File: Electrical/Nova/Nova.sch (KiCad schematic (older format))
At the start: 4 parts

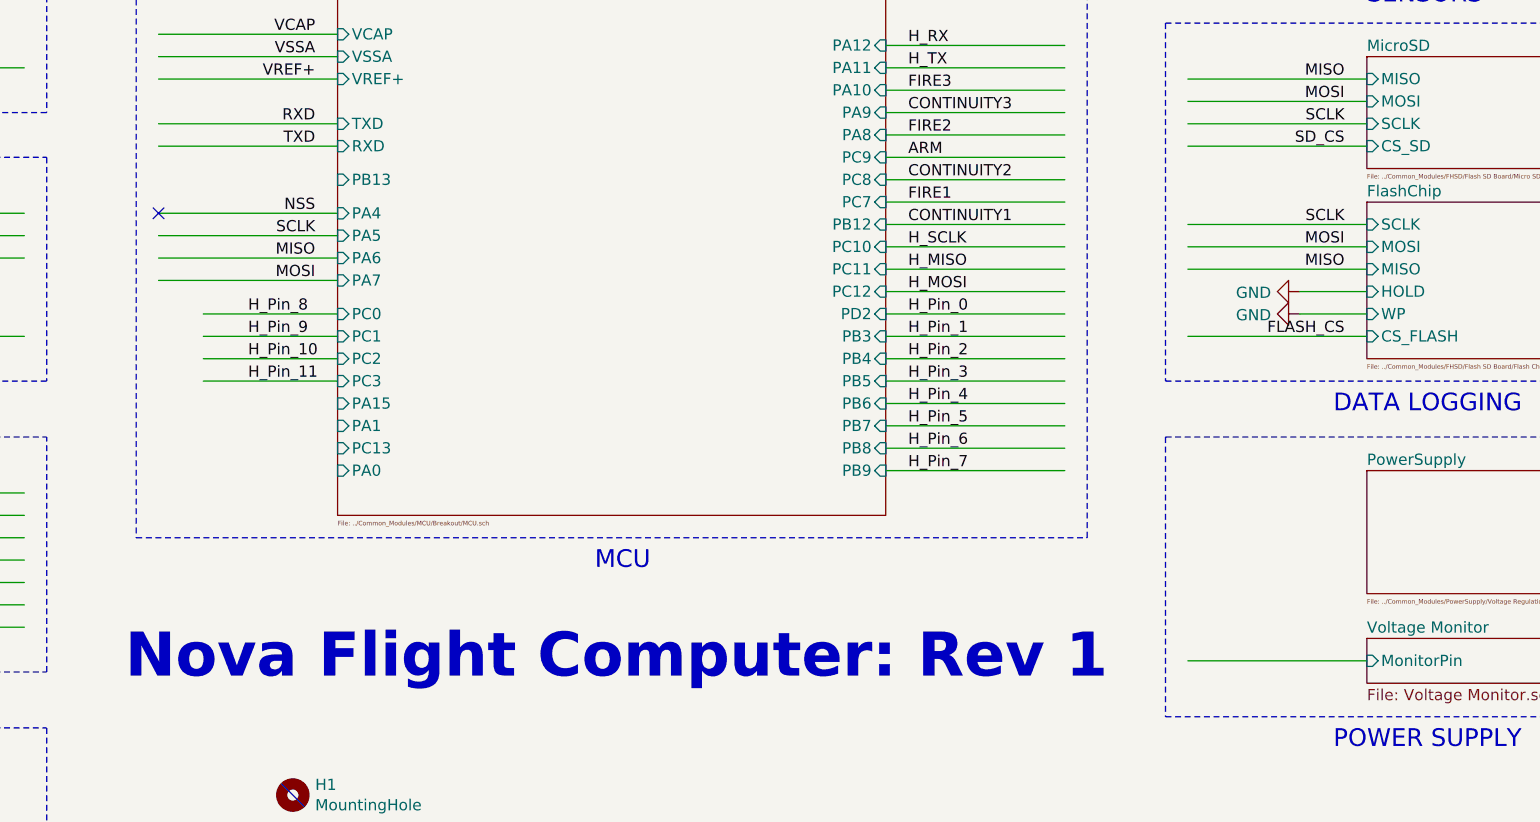
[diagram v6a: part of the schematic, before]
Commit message: Minor Bug Fixes for PCB
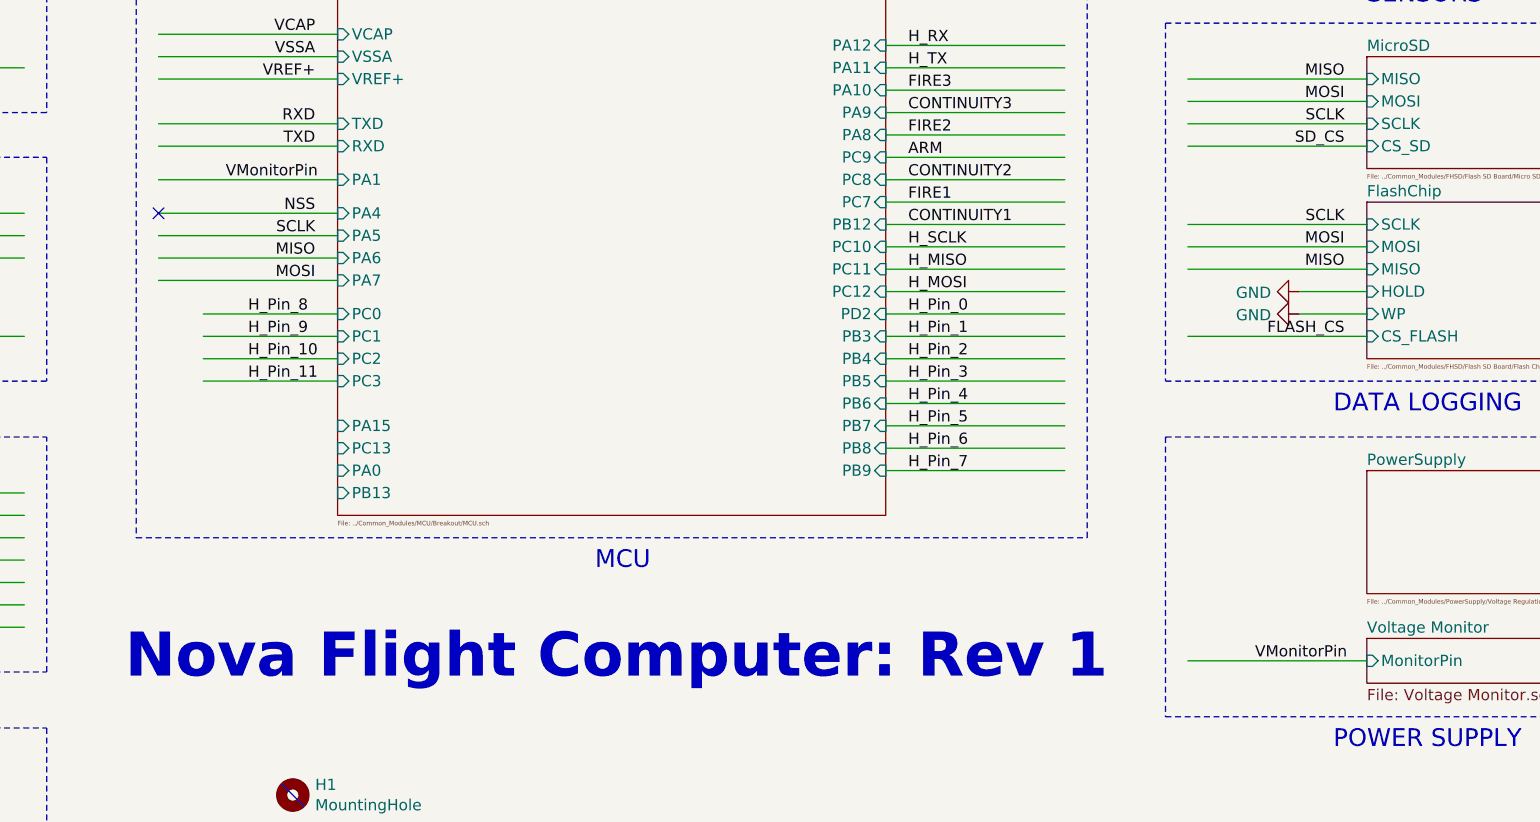
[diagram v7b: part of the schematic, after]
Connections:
- net labels added: VMonitorPin
- wire segments 120 -> 121
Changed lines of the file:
@@
 F25 "PA10" I R 6750 3350 50
 F26 "PB10" I R 6750 2250 50
-F27 "PB13" I L 4300 3750 50
+F27 "PB13" I L 4300 5150 50
 F28 "PB14" I R 6750 2700 50
 F29 "PB15" I R 6750 2800 50
@@
 F43 "PD2" I R 6750 4350 50
 F44 "PA0" I L 4300 5050 50
-F45 "PA1" I L 4300 4850 50
+F45 "PA1" I L 4300 3750 50
 F46 "PA11" I R 6750 3250 50
-F47 "PA15" I L 4300 4750 50
+F47 "PA15" I L 4300 4850 50
 F48 "PB3" I R 6750 4450 50
 F49 "PB4" I R 6750 4550 50
@@
 MOSI
 $Comp
-L power:GND #PWR?
+L power:GND #PWR0122
 U 1 1 5FA3956D
 P 8600 4250
-F 0 "#PWR?" H 8600 4000 50  0001 C CNN
+F 0 "#PWR0122" H 8600 4000 50  0001 C CNN
 F 1 "GND" V 8605 4122 50  0000 R CNN
 F 2 "" H 8600 4250 50  0001 C CNN
@@
 $EndComp
 $Comp
-L power:GND #PWR?
+L power:GND #PWR0123
 U 1 1 5FA39A9B
 P 8600 4350
-F 0 "#PWR?" H 8600 4100 50  0001 C CNN
+F 0 "#PWR0123" H 8600 4100 50  0001 C CNN
 F 1 "GND" V 8605 4222 50  0000 R CNN
 F 2 "" H 8600 4350 50  0001 C CNN
@@
 Wire Wire Line
 	8600 4350 8900 4350
+Text Label 8400 5900 0    50   ~ 0
+VMonitorPin
+Wire Wire Line
+	4300 3750 3500 3750
+Text Label 3800 3750 0    50   ~ 0
+VMonitorPin
 $EndSCHEMATC

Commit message: Electrical REV1
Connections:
- wire segments 121 -> 122
- no-connect marks 7 -> 10
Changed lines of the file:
@@
 Text Label 8800 4450 2    50   ~ 0
 FLASH_CS
-Text Label 8800 3950 2    50   ~ 0
-SCLK
 Text Label 8800 3500 2    50   ~ 0
 SCLK
@@
 F7 "WP" I L 8900 4350 50
 $EndSheet
-Text Label 8800 4150 2    50   ~ 0
-MISO
-Text Label 8800 4050 2    50   ~ 0
-MOSI
 $Comp
 L power:GND #PWR0122
@@
 Text Label 3800 3750 0    50   ~ 0
 VMonitorPin
+Text Label 8500 3950 0    50   ~ 0
+H_SCLK
+Text Label 8500 4050 0    50   ~ 0
+H_MOSI
+Text Label 8500 4150 0    50   ~ 0
+H_MISO
+NoConn ~ 4300 4850
+NoConn ~ 4300 4950
+NoConn ~ 4300 5050
+Text Label 4200 5150 2    50   ~ 0
+FLASH_CS
+Wire Wire Line
+	4300 5150 3500 5150
 $EndSCHEMATC
